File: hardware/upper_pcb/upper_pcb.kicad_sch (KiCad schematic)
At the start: 0 parts

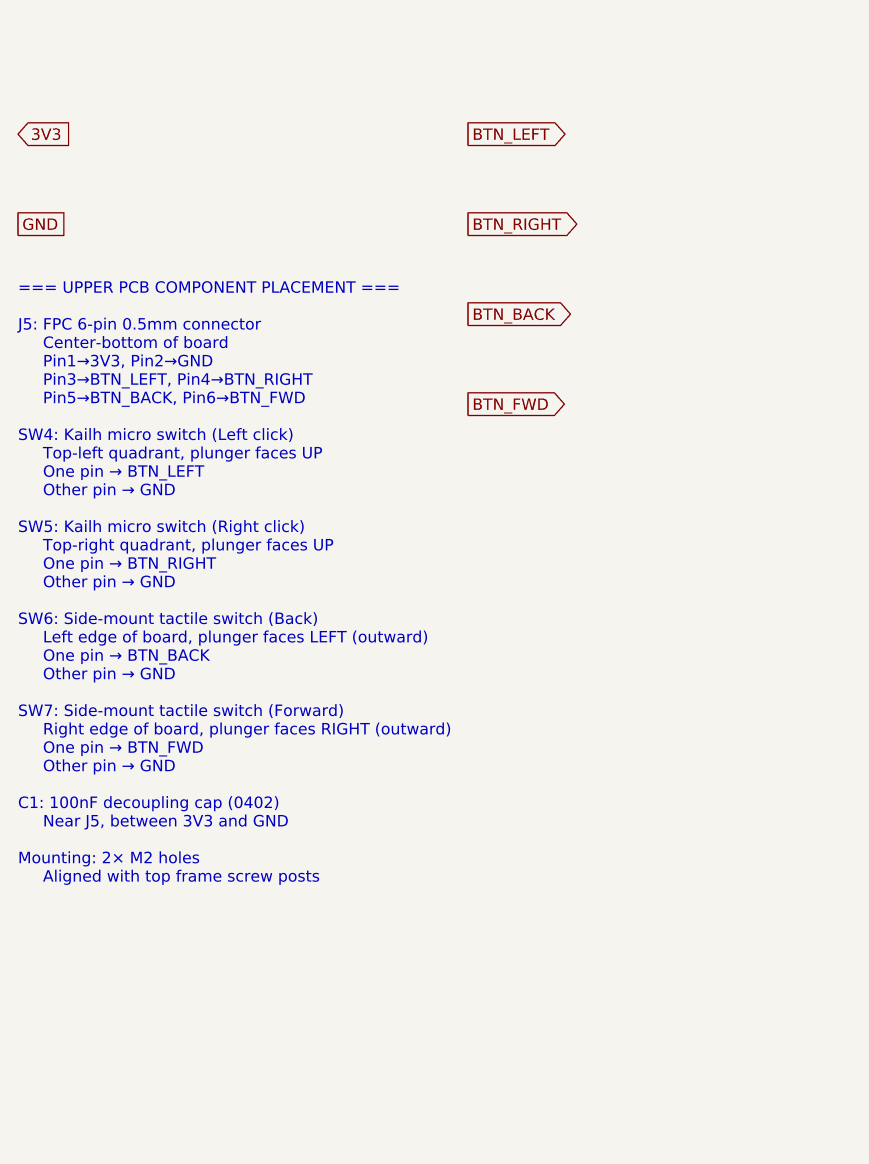
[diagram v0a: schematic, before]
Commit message: fix: move BTN pull-ups (R1-R4) to upper PCB; update schematics + BOM
- upper_pcb.kicad_sch rev 1.2: add R1-R4 (10k pull-ups) + C1 (100nF)
- lower_pcb.kicad_sch rev 1.1: remove R_PU1-R_PU4, keep R_PU5 for JOY_SW
- docs/BOM.md: updated refs to match new placement
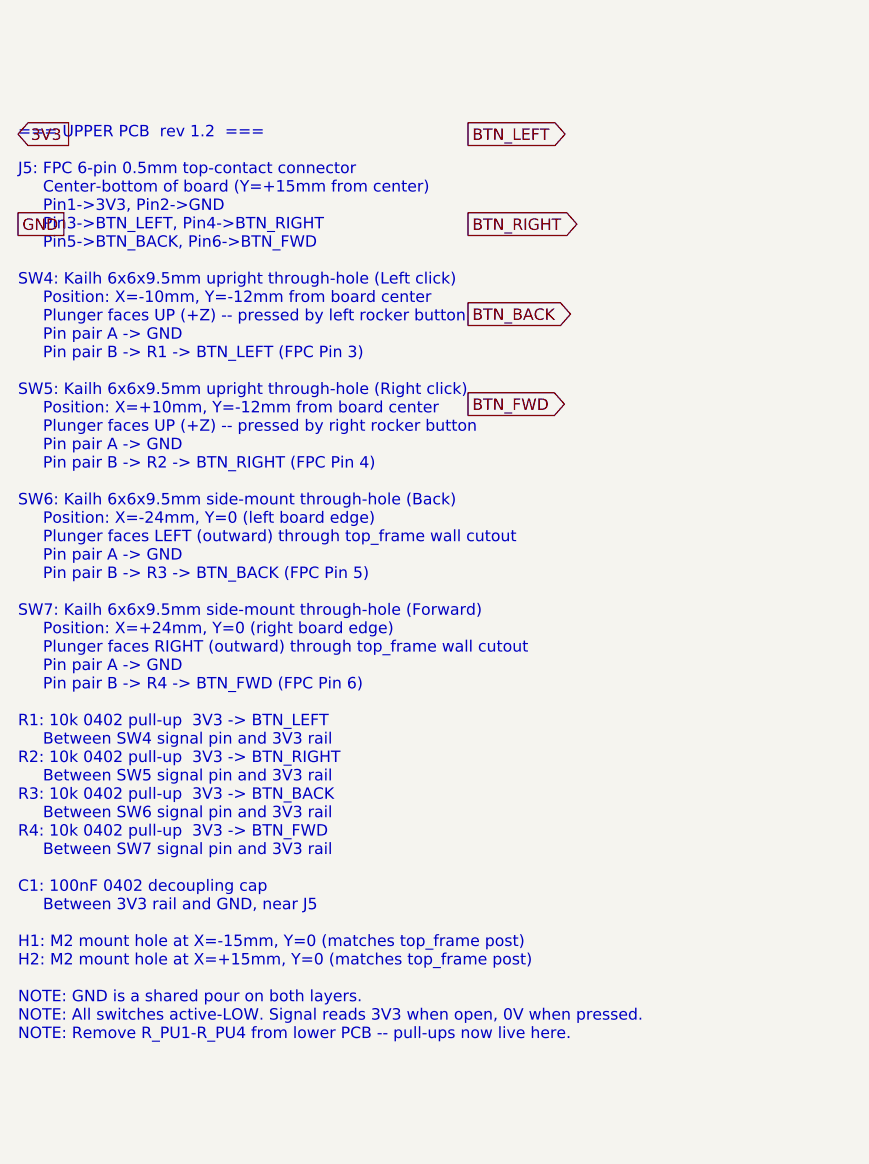
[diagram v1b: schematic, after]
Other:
- note added: "=== UPPER PCB rev 1.2 === J5: FPC 6-pin 0.5mm top-contact connector Center-bottom of board (Y=+15mm from center) Pin1->3V3, Pin2->GND Pin3->BTN_LEFT, Pin4->BTN_RIGHT Pin5->BTN_BACK, Pin6->BTN_FWD SW4: Kailh 6x6x9.5mm upright through-hole (Left click) Position: X=-10mm, Y=-12mm from board center Plunger faces UP (+Z) -- pressed by left rocker button Pin pair A -> GND Pin pair B -> R1 -> BTN_LEFT (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"
- note removed: "=== UPPER PCB COMPONENT PLACEMENT === J5: FPC 6-pin 0.5mm connector Center-bottom of board Pin1→3V3, Pin2→GND Pin3→BTN_LEFT, Pin4→BTN_RIGHT Pin5→BTN_BACK, Pin6→BTN_FWD SW4: Kailh micro switch (Left click) Top-left quadrant, plunger faces UP One pin → BTN_LEFT Other pin → GND SW5: Kailh micro switch (Right click) Top-right quadrant, plunger faces UP One pin → BTN_RIGHT Other pin → GND SW6: Side-mo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"
- title: DaPao Space Mouse — Upper PCB -> DaPao Space Mouse - Upper PCB
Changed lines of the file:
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@@
   (paper "A4")
   (title_block
-    (title "DaPao Space Mouse — Upper PCB")
-    (date "2026-03-11")
-    (rev "1.0")
+    (title "DaPao Space Mouse - Upper PCB")
+    (date "2026-03-20")
+    (rev "1.2")
     (comment 1 "Button board: L/R click + Forward/Back")
-    (comment 2 "Circular PCB ∅54mm, 2-layer, 1.0mm thick")
+    (comment 2 "Circular PCB dia54mm, 2-layer, 1.0mm thick")
+    (comment 3 "Rev 1.2: pull-up resistors moved here from lower PCB")
   )
   ;; ============================================================
-  ;; Simple board: 4 switches + FPC connector + decoupling cap
-  ;; All active-low (pull-ups on lower PCB)
+  ;; 4 switches + 4x 10k pull-ups + 100nF decoupling + FPC
+  ;; All active-low. Pull-ups on this board (not lower PCB).
   ;; ============================================================
-  ;; --- POWER NETS (from FPC) ---
+  ;; --- POWER NETS (from FPC Pin 1/2) ---
   (global_label "3V3" (shape input) (at 30 40 0)
     (effects (font (size 1.27 1.27)))
@@
     (effects (font (size 1.27 1.27)))
   )
-  ;; --- BUTTON NETS ---
-  (global_label "BTN_LEFT" (shape output) (at 80 40 0)
+  ;; --- BUTTON NETS (to FPC Pins 3-6) ---
+  (global_label "BTN_LEFT"  (shape output) (at 80 40 0)
     (effects (font (size 1.27 1.27)))
   )
@@
     (effects (font (size 1.27 1.27)))
   )
-  (global_label "BTN_BACK" (shape output) (at 80 60 0)
+  (global_label "BTN_BACK"  (shape output) (at 80 60 0)
     (effects (font (size 1.27 1.27)))
   )
-  (global_label "BTN_FWD" (shape output) (at 80 70 0)
+  (global_label "BTN_FWD"   (shape output) (at 80 70 0)
     (effects (font (size 1.27 1.27)))
   )
-  ;; --- ANNOTATIONS ---
-  (text "=== UPPER PCB COMPONENT PLACEMENT ===\n\nJ5: FPC 6-pin 0.5mm connector\n     Center-bottom of board\n     Pin1→3V3, Pin2→GND\n     Pin3→BTN_LEFT, Pin4→BTN_RIGHT\n     Pin5→BTN_BACK, Pin6→BTN_FWD\n\nSW4: Kailh micro switch (Left click)\n     Top-left quadrant, plunger faces UP\n     One pin → BTN_LEFT\n     Other pin → GND\n\nSW5: Kailh micro switch (Right click)\n     Top-right quadrant, plunger faces UP\n     One pin → BTN_RIGHT\n     Other pin → GND\n\nSW6: Side-mount tactile switch (Back)\n     Left edge of board, plunger faces LEFT (outward)\n     One pin → BTN_BACK\n     Other pin → GND\n\nSW7: Side-mount tactile switch (Forward)\n     Right edge of board, plunger faces RIGHT (outward)\n     One pin → BTN_FWD\n     Other pin → GND\n\nC1: 100nF decoupling cap (0402)\n     Near J5, between 3V3 and GND\n\nMounting: 2× M2 holes\n     Aligned with top frame screw posts"
+  ;; --- COMPONENT PLACEMENT & WIRING NOTES ---
+  (text "=== UPPER PCB  rev 1.2  ===\n\nJ5: FPC 6-pin 0.5mm top-contact connector\n     Center-bottom of board (Y=+15mm from center)\n     Pin1->3V3, Pin2->GND\n     Pin3->BTN_LEFT, Pin4->BTN_RIGHT\n     Pin5->BTN_BACK, Pin6->BTN_FWD\n\nSW4: Kailh 6x6x9.5mm upright through-hole (Left click)\n     Position: X=-10mm, Y=-12mm from board center\n     Plunger faces UP (+Z) -- pressed by left rocker button\n     Pin pair A -> GND\n     Pin pair B -> R1 -> BTN_LEFT (FPC Pin 3)\n\nSW5: Kailh 6x6x9.5mm upright through-hole (Right click)\n     Position: X=+10mm, Y=-12mm from board center\n     Plunger faces UP (+Z) -- pressed by right rocker button\n     Pin pair A -> GND\n     Pin pair B -> R2 -> BTN_RIGHT (FPC Pin 4)\n\nSW6: Kailh 6x6x9.5mm side-mount through-hole (Back)\n     Position: X=-24mm, Y=0 (left board edge)\n     Plunger faces LEFT (outward) through top_frame wall cutout\n     Pin pair A -> GND\n     Pin pair B -> R3 -> BTN_BACK (FPC Pin 5)\n\nSW7: Kailh 6x6x9.5mm side-mount through-hole (Forward)\n     Position: X=+24mm, Y=0 (right board edge)\n     Plunger faces RIGHT (outward) through top_frame wall cutout\n     Pin pair A -> GND\n     Pin pair B -> R4 -> BTN_FWD (FPC Pin 6)\n\nR1: 10k 0402 pull-up  3V3 -> BTN_LEFT\n     Between SW4 signal pin and 3V3 rail\nR2: 10k 0402 pull-up  3V3 -> BTN_RIGHT\n     Between SW5 signal pin and 3V3 rail\nR3: 10k 0402 pull-up  3V3 -> BTN_BACK\n     Between SW6 signal pin and 3V3 rail\nR4: 10k 0402 pull-up  3V3 -> BTN_FWD\n     Between SW7 signal pin and 3V3 rail\n\nC1: 100nF 0402 decoupling cap\n     Between 3V3 rail and GND, near J5\n\nH1: M2 mount hole at X=-15mm, Y=0 (matches top_frame post)\nH2: M2 mount hole at X=+15mm, Y=0 (matches top_frame post)\n\nNOTE: GND is a shared pour on both layers.\nNOTE: All switches active-LOW. Signal reads 3V3 when open, 0V when pressed.\nNOTE: Remove R_PU1-R_PU4 from lower PCB -- pull-ups now live here."
     (at 30 90 0)
     (effects (font (size 1.27 1.27)) (justify left))

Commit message: feat: upgrade upper PCB switches to Kailh GM 8.0 + Blue Dot (rev 1.3)
- SW4/SW5: Kailh GM 8.0 (3-pin THT, Cherry-style, 12.8x5.8mm)
  plunger UP, pressed by rocker buttons
- SW6/SW7: Kailh Blue Dot SMT side-button (~8.75mm)
  plunger faces outward L/R through top_frame cutouts
- R1-R4: 10k pull-ups retained (one per BTN signal, active-low)
- C1: 100nF decoupling retained
- NC pins on GM 8.0 left floating
- BOM updated with new part refs and sources
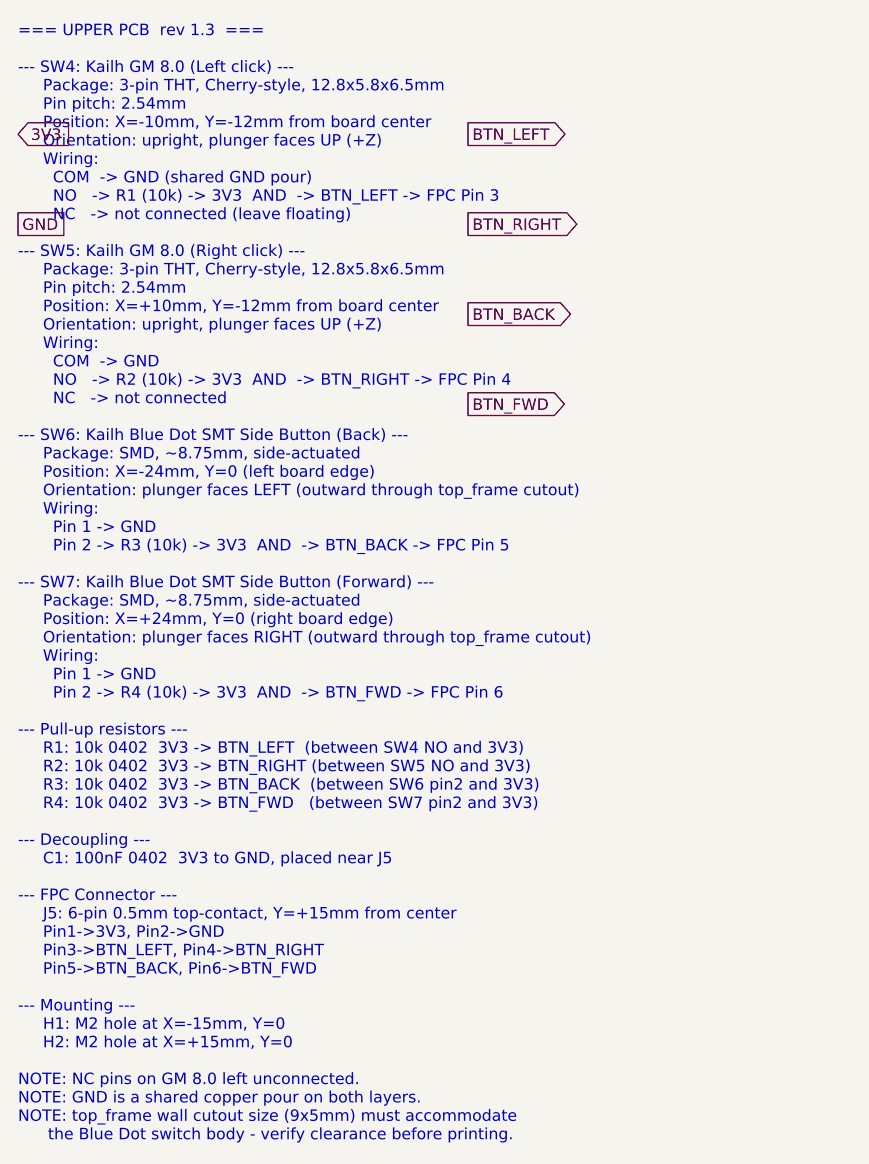
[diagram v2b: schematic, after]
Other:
- note added: "=== UPPER PCB rev 1.3 === --- SW4: Kailh GM 8.0 (Left click) --- Package: 3-pin THT, Cherry-style, 12.8x5.8x6.5mm Pin pitch: 2.54mm Position: X=-10mm, Y=-12mm from board center Orientation: upright, plunger faces UP (+Z) Wiring: COM -> GND (shared GND pour) NO -> R1 (10k) -> 3V3 AND -> BTN_LEFT -> FPC Pin 3 NC -> not connected (leave floating) --- SW5: Kailh GM 8.0 (Right click) --- Package: 3-pi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"
- note removed: "=== UPPER PCB rev 1.2 === J5: FPC 6-pin 0.5mm top-contact connector Center-bottom of board (Y=+15mm from center) Pin1->3V3, Pin2->GND Pin3->BTN_LEFT, Pin4->BTN_RIGHT Pin5->BTN_BACK, Pin6->BTN_FWD SW4: Kailh 6x6x9.5mm upright through-hole (Left click) Position: X=-10mm, Y=-12mm from board center Plunger faces UP (+Z) -- pressed by left rocker button Pin pair A -> GND Pin pair B -> R1 -> BTN_LEFT (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"
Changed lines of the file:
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@@
     (title "DaPao Space Mouse - Upper PCB")
     (date "2026-03-20")
-    (rev "1.2")
+    (rev "1.3")
     (comment 1 "Button board: L/R click + Forward/Back")
     (comment 2 "Circular PCB dia54mm, 2-layer, 1.0mm thick")
-    (comment 3 "Rev 1.2: pull-up resistors moved here from lower PCB")
+    (comment 3 "Rev 1.3: SW4/SW5 -> Kailh GM 8.0 (3-pin THT). SW6/SW7 -> Kailh Blue Dot SMT side-mount.")
   )
   ;; ============================================================
-  ;; 4 switches + 4x 10k pull-ups + 100nF decoupling + FPC
-  ;; All active-low. Pull-ups on this board (not lower PCB).
+  ;; Components:
+  ;;   SW4/SW5: Kailh GM 8.0 micro switch (3-pin, Cherry-style)
+  ;;            12.8 x 5.8 x 6.5mm, 2.54mm pin pitch
+  ;;            Pins: COM (common), NO (normally open), NC (normally closed)
+  ;;            We use COM + NO only (active-low with pull-up)
+  ;;
+  ;;   SW6/SW7: Kailh Blue Dot SMT side-button micro switch
+  ;;            ~8.75mm, SMD, plunger faces outward (left/right)
+  ;;            2-pin: signal + GND
+  ;;
+  ;;   R1-R4:   10k 0402 pull-ups (3V3 -> each BTN signal)
+  ;;   C1:      100nF 0402 decoupling on 3V3
+  ;;   J5:      FPC 6-pin 0.5mm top-contact (cable to lower PCB)
   ;; ============================================================
-  ;; --- POWER NETS (from FPC Pin 1/2) ---
+  ;; --- POWER NETS ---
   (global_label "3V3" (shape input) (at 30 40 0)
     (effects (font (size 1.27 1.27)))
@@
     (effects (font (size 1.27 1.27)))
   )
-  ;; --- BUTTON NETS (to FPC Pins 3-6) ---
-  (global_label "BTN_LEFT"  (shape output) (at 80 40 0)
-    (effects (font (size 1.27 1.27)))
-  )
-  (global_label "BTN_RIGHT" (shape output) (at 80 50 0)
-    (effects (font (size 1.27 1.27)))
-  )
-  (global_label "BTN_BACK"  (shape output) (at 80 60 0)
-    (effects (font (size 1.27 1.27)))
-  )
-  (global_label "BTN_FWD"   (shape output) (at 80 70 0)
-    (effects (font (size 1.27 1.27)))
-  )
-  ;; --- COMPONENT PLACEMENT & WIRING NOTES ---
-  (text "=== UPPER PCB  rev 1.2  ===\n\nJ5: FPC 6-pin 0.5mm top-contact connector\n     Center-bottom of board (Y=+15mm from center)\n     Pin1->3V3, Pin2->GND\n     Pin3->BTN_LEFT, Pin4->BTN_RIGHT\n     Pin5->BTN_BACK, Pin6->BTN_FWD\n\nSW4: Kailh 6x6x9.5mm upright through-hole (Left click)\n     Position: X=-10mm, Y=-12mm from board center\n     Plunger faces UP (+Z) -- pressed by left rocker button\n     Pin pair A -> GND\n     Pin pair B -> R1 -> BTN_LEFT (FPC Pin 3)\n\nSW5: Kailh 6x6x9.5mm upright through-hole (Right click)\n     Position: X=+10mm, Y=-12mm from board center\n     Plunger faces UP (+Z) -- pressed by right rocker button\n     Pin pair A -> GND\n     Pin pair B -> R2 -> BTN_RIGHT (FPC Pin 4)\n\nSW6: Kailh 6x6x9.5mm side-mount through-hole (Back)\n     Position: X=-24mm, Y=0 (left board edge)\n     Plunger faces LEFT (outward) through top_frame wall cutout\n     Pin pair A -> GND\n     Pin pair B -> R3 -> BTN_BACK (FPC Pin 5)\n\nSW7: Kailh 6x6x9.5mm side-mount through-hole (Forward)\n     Position: X=+24mm, Y=0 (right board edge)\n     Plunger faces RIGHT (outward) through top_frame wall cutout\n     Pin pair A -> GND\n     Pin pair B -> R4 -> BTN_FWD (FPC Pin 6)\n\nR1: 10k 0402 pull-up  3V3 -> BTN_LEFT\n     Between SW4 signal pin and 3V3 rail\nR2: 10k 0402 pull-up  3V3 -> BTN_RIGHT\n     Between SW5 signal pin and 3V3 rail\nR3: 10k 0402 pull-up  3V3 -> BTN_BACK\n     Between SW6 signal pin and 3V3 rail\nR4: 10k 0402 pull-up  3V3 -> BTN_FWD\n     Between SW7 signal pin and 3V3 rail\n\nC1: 100nF 0402 decoupling cap\n     Between 3V3 rail and GND, near J5\n\nH1: M2 mount hole at X=-15mm, Y=0 (matches top_frame post)\nH2: M2 mount hole at X=+15mm, Y=0 (matches top_frame post)\n\nNOTE: GND is a shared pour on both layers.\nNOTE: All switches active-LOW. Signal reads 3V3 when open, 0V when pressed.\nNOTE: Remove R_PU1-R_PU4 from lower PCB -- pull-ups now live here."
+  ;; --- BUTTON SIGNAL NETS ---
+  (global_label "BTN_LEFT"  (shape output) (at 80 40 0) (effects (font (size 1.27 1.27))))
+  (global_label "BTN_RIGHT" (shape output) (at 80 50 0) (effects (font (size 1.27 1.27))))
+  (global_label "BTN_BACK"  (shape output) (at 80 60 0) (effects (font (size 1.27 1.27))))
+  (global_label "BTN_FWD"   (shape output) (at 80 70 0) (effects (font (size 1.27 1.27))))
+  ;; --- PLACEMENT & WIRING NOTES ---
+  (text "=== UPPER PCB  rev 1.3  ===\n\n--- SW4: Kailh GM 8.0 (Left click) ---\n     Package: 3-pin THT, Cherry-style, 12.8x5.8x6.5mm\n     Pin pitch: 2.54mm\n     Position: X=-10mm, Y=-12mm from board center\n     Orientation: upright, plunger faces UP (+Z)\n     Wiring:\n       COM  -> GND (shared GND pour)\n       NO   -> R1 (10k) -> 3V3  AND  -> BTN_LEFT -> FPC Pin 3\n       NC   -> not connected (leave floating)\n\n--- SW5: Kailh GM 8.0 (Right click) ---\n     Package: 3-pin THT, Cherry-style, 12.8x5.8x6.5mm\n     Pin pitch: 2.54mm\n     Position: X=+10mm, Y=-12mm from board center\n     Orientation: upright, plunger faces UP (+Z)\n     Wiring:\n       COM  -> GND\n       NO   -> R2 (10k) -> 3V3  AND  -> BTN_RIGHT -> FPC Pin 4\n       NC   -> not connected\n\n--- SW6: Kailh Blue Dot SMT Side Button (Back) ---\n     Package: SMD, ~8.75mm, side-actuated\n     Position: X=-24mm, Y=0 (left board edge)\n     Orientation: plunger faces LEFT (outward through top_frame cutout)\n     Wiring:\n       Pin 1 -> GND\n       Pin 2 -> R3 (10k) -> 3V3  AND  -> BTN_BACK -> FPC Pin 5\n\n--- SW7: Kailh Blue Dot SMT Side Button (Forward) ---\n     Package: SMD, ~8.75mm, side-actuated\n     Position: X=+24mm, Y=0 (right board edge)\n     Orientation: plunger faces RIGHT (outward through top_frame cutout)\n     Wiring:\n       Pin 1 -> GND\n       Pin 2 -> R4 (10k) -> 3V3  AND  -> BTN_FWD -> FPC Pin 6\n\n--- Pull-up resistors ---\n     R1: 10k 0402  3V3 -> BTN_LEFT  (between SW4 NO and 3V3)\n     R2: 10k 0402  3V3 -> BTN_RIGHT (between SW5 NO and 3V3)\n     R3: 10k 0402  3V3 -> BTN_BACK  (between SW6 pin2 and 3V3)\n     R4: 10k 0402  3V3 -> BTN_FWD   (between SW7 pin2 and 3V3)\n\n--- Decoupling ---\n     C1: 100nF 0402  3V3 to GND, placed near J5\n\n--- FPC Connector ---\n     J5: 6-pin 0.5mm top-contact, Y=+15mm from center\n     Pin1->3V3, Pin2->GND\n     Pin3->BTN_LEFT, Pin4->BTN_RIGHT\n     Pin5->BTN_BACK, Pin6->BTN_FWD\n\n--- Mounting ---\n     H1: M2 hole at X=-15mm, Y=0\n     H2: M2 hole at X=+15mm, Y=0\n\nNOTE: NC pins on GM 8.0 left unconnected.\nNOTE: GND is a shared copper pour on both layers.\nNOTE: top_frame wall cutout size (9x5mm) must accommodate\n      the Blue Dot switch body - verify clearance before printing."
     (at 30 90 0)
     (effects (font (size 1.27 1.27)) (justify left))
